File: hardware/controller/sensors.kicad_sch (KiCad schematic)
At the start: 10 parts, among them J5 Conn_01x07, U8 MPU-6050

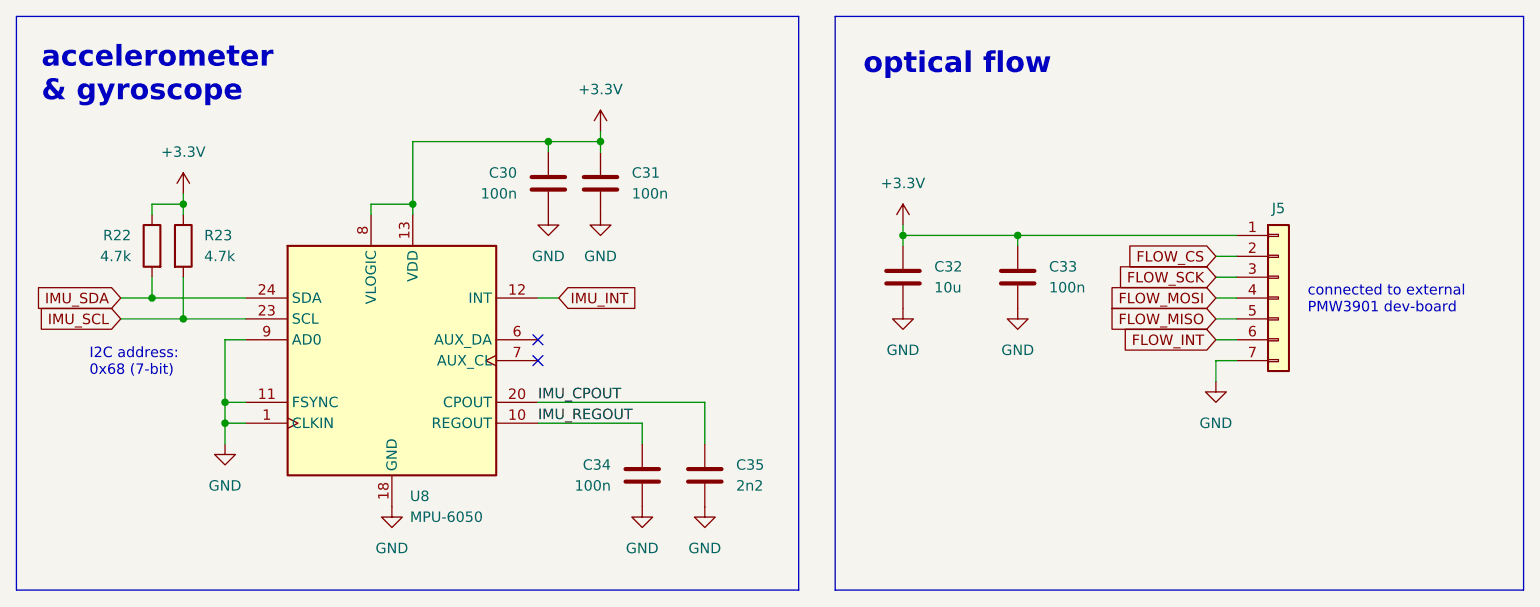
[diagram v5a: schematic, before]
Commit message: back to LM2105, remove USB-C from STM
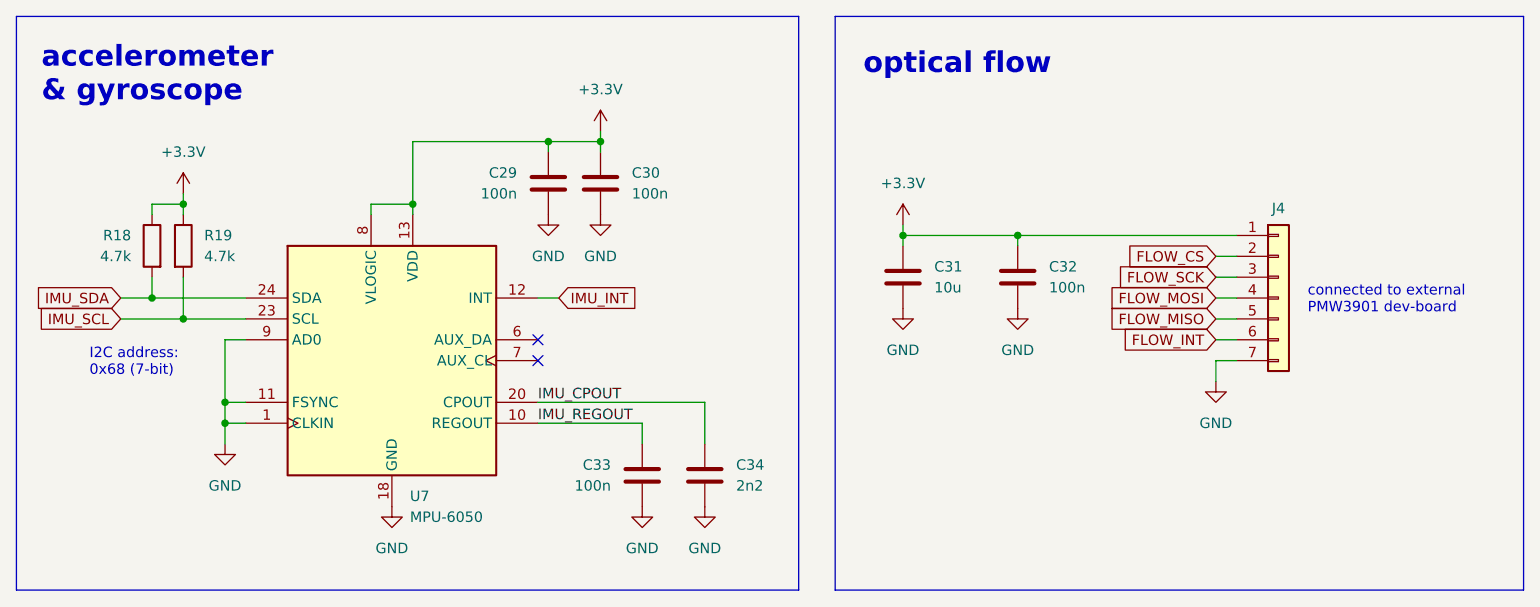
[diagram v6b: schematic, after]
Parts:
- renumbered C30 to C29, C31 to C30, C32 to C31, C33 to C32, C34 to C33, C35 to C34, J5 to J4, R22 to R18, R23 to R19, U8 to U7
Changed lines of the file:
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@@
 		(dnp no)
 		(fields_autoplaced yes)
-		(property "Reference" "#PWR073"
+		(property "Reference" "#PWR067"
 			(at 111.76 68.58 0)
 			(effects
@@
 			(project "controller"
 				(path "/b81e4285-7ba7-4843-ab37-49bb8c6c135f/9b959a7f-7785-4fbc-97ae-e71bdac42a24"
-					(reference "#PWR073")
+					(reference "#PWR067")
 					(unit 1)
 				)
@@
 		(on_board yes)
 		(dnp no)
-		(property "Reference" "U8"
+		(property "Reference" "U7"
 			(at 88.5541 109.22 0)
 			(effects
@@
 			(project ""
 				(path "/b81e4285-7ba7-4843-ab37-49bb8c6c135f/9b959a7f-7785-4fbc-97ae-e71bdac42a24"
-					(reference "U8")
+					(reference "U7")
 					(unit 1)
 				)
@@
 		(dnp no)
 		(fields_autoplaced yes)
-		(property "Reference" "C30"
+		(property "Reference" "C29"
 			(at 101.6 69.8499 0)
 			(effects
@@
 			(project "controller"
 				(path "/b81e4285-7ba7-4843-ab37-49bb8c6c135f/9b959a7f-7785-4fbc-97ae-e71bdac42a24"
-					(reference "C30")
+					(reference "C29")
 					(unit 1)
 				)
@@
 		(on_board yes)
 		(dnp no)
-		(property "Reference" "C34"
+		(property "Reference" "C33"
 			(at 113.03 105.4099 0)
 			(effects
@@
 			(project "controller"
 				(path "/b81e4285-7ba7-4843-ab37-49bb8c6c135f/9b959a7f-7785-4fbc-97ae-e71bdac42a24"
-					(reference "C34")
+					(reference "C33")
 					(unit 1)
 				)
@@
 		(dnp no)
 		(fields_autoplaced yes)
-		(property "Reference" "#PWR083"
+		(property "Reference" "#PWR077"
 			(at 116.84 116.84 0)
 			(effects
@@
 			(project "controller"
 				(path "/b81e4285-7ba7-4843-ab37-49bb8c6c135f/9b959a7f-7785-4fbc-97ae-e71bdac42a24"
-					(reference "#PWR083")
+					(reference "#PWR077")
 					(unit 1)
 				)
@@
 		(dnp no)
 		(fields_autoplaced yes)
-		(property "Reference" "R23"
+		(property "Reference" "R19"
 			(at 63.5 77.4699 0)
 			(effects
@@
 			(project "controller"
 				(path "/b81e4285-7ba7-4843-ab37-49bb8c6c135f/9b959a7f-7785-4fbc-97ae-e71bdac42a24"
-					(reference "R23")
+					(reference "R19")
 					(unit 1)
 				)
@@
 		(on_board yes)
 		(dnp no)
-		(property "Reference" "C32"
+		(property "Reference" "C31"
 			(at 152.4 81.2799 0)
 			(effects
@@
 			(project "controller"
 				(path "/b81e4285-7ba7-4843-ab37-49bb8c6c135f/9b959a7f-7785-4fbc-97ae-e71bdac42a24"
-					(reference "C32")
+					(reference "C31")
 					(unit 1)
 				)
@@
 		(dnp no)
 		(fields_autoplaced yes)
-		(property "Reference" "#PWR080"
+		(property "Reference" "#PWR074"
 			(at 186.69 101.6 0)
 			(effects
@@
 			(project "controller"
 				(path "/b81e4285-7ba7-4843-ab37-49bb8c6c135f/9b959a7f-7785-4fbc-97ae-e71bdac42a24"
-					(reference "#PWR080")
+					(reference "#PWR074")
 					(unit 1)
 				)
@@
 		(dnp no)
 		(fields_autoplaced yes)
-		(property "Reference" "C31"
+		(property "Reference" "C30"
 			(at 115.57 69.8499 0)
 			(effects
@@
 			(project "controller"
 				(path "/b81e4285-7ba7-4843-ab37-49bb8c6c135f/9b959a7f-7785-4fbc-97ae-e71bdac42a24"
-					(reference "C31")
+					(reference "C30")
 					(unit 1)
 				)
@@
 		(dnp no)
 		(fields_autoplaced yes)
-		(property "Reference" "#PWR079"
+		(property "Reference" "#PWR073"
 			(at 162.56 92.71 0)
 			(effects
@@
 			(project "controller"
 				(path "/b81e4285-7ba7-4843-ab37-49bb8c6c135f/9b959a7f-7785-4fbc-97ae-e71bdac42a24"
-					(reference "#PWR079")
+					(reference "#PWR073")
 					(unit 1)
 				)
@@
 		(dnp no)
 		(fields_autoplaced yes)
-		(property "Reference" "#PWR074"
+		(property "Reference" "#PWR068"
 			(at 60.96 76.2 0)
 			(effects
@@
 			(project "controller"
 				(path "/b81e4285-7ba7-4843-ab37-49bb8c6c135f/9b959a7f-7785-4fbc-97ae-e71bdac42a24"
-					(reference "#PWR074")
+					(reference "#PWR068")
 					(unit 1)
 				)
@@
 		(on_board yes)
 		(dnp no)
-		(property "Reference" "C33"
+		(property "Reference" "C32"
 			(at 166.37 81.2799 0)
 			(effects
@@
 			(project "controller"
 				(path "/b81e4285-7ba7-4843-ab37-49bb8c6c135f/9b959a7f-7785-4fbc-97ae-e71bdac42a24"
-					(reference "C33")
+					(reference "C32")
 					(unit 1)
 				)
@@
 		(dnp no)
 		(fields_autoplaced yes)
-		(property "Reference" "#PWR075"
+		(property "Reference" "#PWR069"
 			(at 105.41 81.28 0)
 			(effects
@@
 			(project "controller"
 				(path "/b81e4285-7ba7-4843-ab37-49bb8c6c135f/9b959a7f-7785-4fbc-97ae-e71bdac42a24"
-					(reference "#PWR075")
+					(reference "#PWR069")
 					(unit 1)
 				)
@@
 		(dnp no)
 		(fields_autoplaced yes)
-		(property "Reference" "C35"
+		(property "Reference" "C34"
 			(at 128.27 105.4099 0)
 			(effects
@@
 			(project "controller"
 				(path "/b81e4285-7ba7-4843-ab37-49bb8c6c135f/9b959a7f-7785-4fbc-97ae-e71bdac42a24"
-					(reference "C35")
+					(reference "C34")
 					(unit 1)
 				)
@@
 		(on_board yes)
 		(dnp no)
-		(property "Reference" "J5"
+		(property "Reference" "J4"
 			(at 194.31 74.168 0)
 			(effects
@@
 			(project ""
 				(path "/b81e4285-7ba7-4843-ab37-49bb8c6c135f/9b959a7f-7785-4fbc-97ae-e71bdac42a24"
-					(reference "J5")
+					(reference "J4")
 					(unit 1)
 				)
@@
 		(dnp no)
 		(fields_autoplaced yes)
-		(property "Reference" "#PWR082"
+		(property "Reference" "#PWR076"
 			(at 86.36 116.84 0)
 			(effects
@@
 			(project "controller"
 				(path "/b81e4285-7ba7-4843-ab37-49bb8c6c135f/9b959a7f-7785-4fbc-97ae-e71bdac42a24"
-					(reference "#PWR082")
+					(reference "#PWR076")
 					(unit 1)
 				)
@@
 		(dnp no)
 		(fields_autoplaced yes)
-		(property "Reference" "#PWR081"
+		(property "Reference" "#PWR075"
 			(at 66.04 109.22 0)
 			(effects
@@
 			(project "controller"
 				(path "/b81e4285-7ba7-4843-ab37-49bb8c6c135f/9b959a7f-7785-4fbc-97ae-e71bdac42a24"
-					(reference "#PWR081")
+					(reference "#PWR075")
 					(unit 1)
 				)
@@
 		(dnp no)
 		(fields_autoplaced yes)
-		(property "Reference" "#PWR076"
+		(property "Reference" "#PWR070"
 			(at 111.76 81.28 0)
 			(effects
@@
 			(project "controller"
 				(path "/b81e4285-7ba7-4843-ab37-49bb8c6c135f/9b959a7f-7785-4fbc-97ae-e71bdac42a24"
-					(reference "#PWR076")
+					(reference "#PWR070")
 					(unit 1)
 				)
@@
 		(dnp no)
 		(fields_autoplaced yes)
-		(property "Reference" "#PWR078"
+		(property "Reference" "#PWR072"
 			(at 148.59 92.71 0)
 			(effects
@@
 			(project "controller"
 				(path "/b81e4285-7ba7-4843-ab37-49bb8c6c135f/9b959a7f-7785-4fbc-97ae-e71bdac42a24"
-					(reference "#PWR078")
+					(reference "#PWR072")
 					(unit 1)
 				)
@@
 		(dnp no)
 		(fields_autoplaced yes)
-		(property "Reference" "#PWR077"
+		(property "Reference" "#PWR071"
 			(at 148.59 80.01 0)
 			(effects
@@
 			(project "controller"
 				(path "/b81e4285-7ba7-4843-ab37-49bb8c6c135f/9b959a7f-7785-4fbc-97ae-e71bdac42a24"
-					(reference "#PWR077")
+					(reference "#PWR071")
 					(unit 1)
 				)
@@
 		(on_board yes)
 		(dnp no)
-		(property "Reference" "R22"
+		(property "Reference" "R18"
 			(at 54.61 77.4699 0)
 			(effects
@@
 			(project "controller"
 				(path "/b81e4285-7ba7-4843-ab37-49bb8c6c135f/9b959a7f-7785-4fbc-97ae-e71bdac42a24"
-					(reference "R22")
+					(reference "R18")
 					(unit 1)
 				)
@@
 		(dnp no)
 		(fields_autoplaced yes)
-		(property "Reference" "#PWR084"
+		(property "Reference" "#PWR078"
 			(at 124.46 116.84 0)
 			(effects
@@
 			(project "controller"
 				(path "/b81e4285-7ba7-4843-ab37-49bb8c6c135f/9b959a7f-7785-4fbc-97ae-e71bdac42a24"
-					(reference "#PWR084")
-					(unit 1)
-				)
+					(reference "#PWR078")
+					(unit 1)
+				)
